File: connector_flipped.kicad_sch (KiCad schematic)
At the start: 4 parts, among them J1 Screw_Terminal_01x04

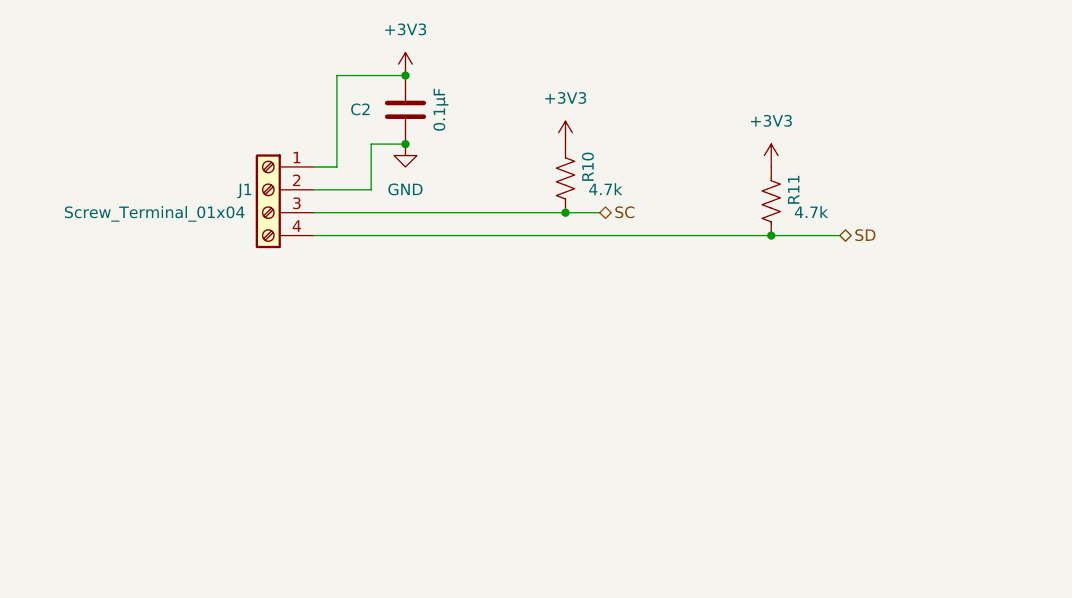
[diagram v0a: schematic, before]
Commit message: four sensor connectors flipped to the way they should be installed.
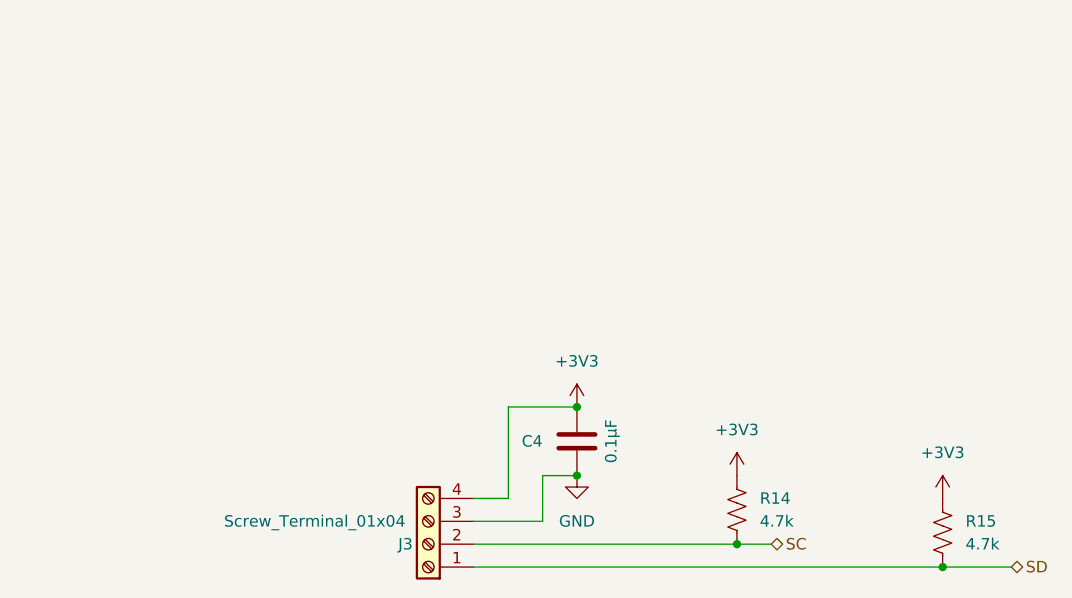
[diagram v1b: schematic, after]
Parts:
- removed C2: 0.1µF, ProjectLib:C_0402_1005Metric, symbol ProjectLib:C
- removed J1: Screw_Terminal_01x04, ProjectLib:TerminalBlock_Phoenix_MPT-0,5-4-2.54_1x04_P2.54mm_Horizontal, symbol ProjectLib:Screw_Terminal_01x04
- removed R10, R11: 4.7k, ProjectLib:R_0402_1005Metric, symbol ProjectLib:R_US
- added C4: 0.1µF, ProjectLib:C_0402_1005Metric, symbol ProjectLib:C
- added J3: Screw_Terminal_01x04, ProjectLib:TerminalBlock_Phoenix_MPT-0,5-4-2.54_1x04_P2.54mm_Horizontal, symbol ProjectLib:Screw_Terminal_01x04
- added R14, R15: 4.7k, ProjectLib:R_0402_1005Metric, symbol ProjectLib:R_US
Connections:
- net +3V3: now also C4.1, J3.4 (Pin_4), R14.1, R15.1
- net GND: now also C4.2, J3.3 (Pin_3)
- net SC: now also J3.2 (Pin_2), R14.2
- net SD: now also J3.1 (Pin_1), R15.2

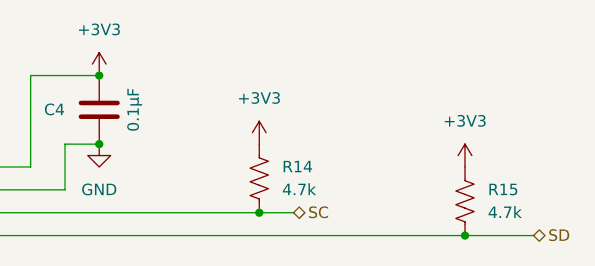
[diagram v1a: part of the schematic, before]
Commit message: changed single 10k pull-up to 4.7k like others. Renumbered components to fill numbering gaps.
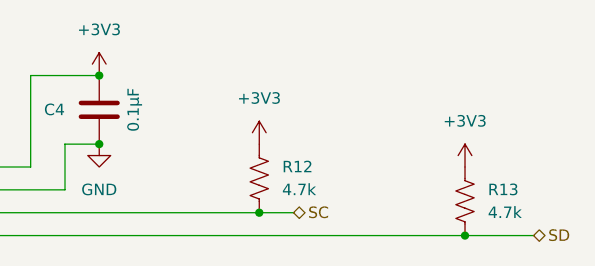
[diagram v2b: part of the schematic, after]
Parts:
- renumbered R14 to R12, R15 to R13
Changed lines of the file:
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@@
 		(dnp no)
 		(fields_autoplaced yes)
-		(property "Reference" "R14"
+		(property "Reference" "R12"
 			(at 124.46 78.7399 0)
 			(effects
@@
 			(project "multiplexI2C"
 				(path "/0c2d0c14-8850-4a30-bb78-b2f40cb442ba/0ffcdb2c-d74e-4b7d-b16c-7be1edbff217"
-					(reference "R24")
+					(reference "R22")
 					(unit 1)
 				)
 				(path "/0c2d0c14-8850-4a30-bb78-b2f40cb442ba/a879a04a-2836-4e79-a27d-1b46398578a8"
-					(reference "R22")
+					(reference "R20")
 					(unit 1)
 				)
 				(path "/0c2d0c14-8850-4a30-bb78-b2f40cb442ba/c4c0e226-9808-439f-a0d2-8470ea18ef3d"
+					(reference "R12")
+					(unit 1)
+				)
+				(path "/0c2d0c14-8850-4a30-bb78-b2f40cb442ba/fd54f7e6-e57e-45a8-af7b-068cfabb882f"
 					(reference "R14")
-					(unit 1)
-				)
-				(path "/0c2d0c14-8850-4a30-bb78-b2f40cb442ba/fd54f7e6-e57e-45a8-af7b-068cfabb882f"
-					(reference "R16")
 					(unit 1)
 				)
@@
 		(dnp no)
 		(fields_autoplaced yes)
-		(property "Reference" "R15"
+		(property "Reference" "R13"
 			(at 147.32 81.2799 0)
 			(effects
@@
 			(project "multiplexI2C"
 				(path "/0c2d0c14-8850-4a30-bb78-b2f40cb442ba/0ffcdb2c-d74e-4b7d-b16c-7be1edbff217"
-					(reference "R25")
+					(reference "R23")
 					(unit 1)
 				)
 				(path "/0c2d0c14-8850-4a30-bb78-b2f40cb442ba/a879a04a-2836-4e79-a27d-1b46398578a8"
-					(reference "R23")
+					(reference "R21")
 					(unit 1)
 				)
 				(path "/0c2d0c14-8850-4a30-bb78-b2f40cb442ba/c4c0e226-9808-439f-a0d2-8470ea18ef3d"
+					(reference "R13")
+					(unit 1)
+				)
+				(path "/0c2d0c14-8850-4a30-bb78-b2f40cb442ba/fd54f7e6-e57e-45a8-af7b-068cfabb882f"
 					(reference "R15")
 					(unit 1)
 				)
-				(path "/0c2d0c14-8850-4a30-bb78-b2f40cb442ba/fd54f7e6-e57e-45a8-af7b-068cfabb882f"
-					(reference "R17")
-					(unit 1)
-				)

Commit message: cleaned up fab layer annotation.
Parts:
- C4, R12, R13: Notes (none) -> or equivalent
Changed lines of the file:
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@@
 			)
 		)
-		(property "Notes" ""
+		(property "Notes" "or equivalent"
+			(at 104.14 72.39 0)
+			(effects
+				(font
+					(size 1.27 1.27)
+				)
+				(hide yes)
+			)
+		)
+		(property "Manuf Part" ""
+			(at 104.14 72.39 0)
+			(effects
+				(font
+					(size 1.27 1.27)
+				)
+				(hide yes)
+			)
+		)
+		(property "Manuf Series" ""
 			(at 104.14 72.39 0)
 			(effects
@@
 		)
 		(property "Notes" "or equivalent"
+			(at 87.63 83.82 0)
+			(effects
+				(font
+					(size 1.27 1.27)
+				)
+				(hide yes)
+			)
+		)
+		(property "Manuf Part" ""
+			(at 87.63 83.82 0)
+			(effects
+				(font
+					(size 1.27 1.27)
+				)
+				(hide yes)
+			)
+		)
+		(property "Manuf Series" ""
 			(at 87.63 83.82 0)
 			(effects
@@
 			)
 		)
-		(property "Notes" ""
+		(property "Notes" "or equivalent"
+			(at 121.92 80.01 0)
+			(effects
+				(font
+					(size 1.27 1.27)
+				)
+				(hide yes)
+			)
+		)
+		(property "Manuf Part" ""
+			(at 121.92 80.01 0)
+			(effects
+				(font
+					(size 1.27 1.27)
+				)
+				(hide yes)
+			)
+		)
+		(property "Manuf Series" ""
 			(at 121.92 80.01 0)
 			(effects
@@
 			)
 		)
-		(property "Notes" ""
-			(at 144.78 82.55 0)
-			(effects
+		(property "Notes" "or equivalent"
+			(at 144.78 82.55 0)
+			(effects
+				(font
+					(size 1.27 1.27)
+				)
+				(hide yes)
+			)
+		)
+		(property "Manuf Part" ""
+			(at 144.78 82.55 0)
+			(effects
+				(font
+					(size 1.27 1.27)
+				)
+				(hide yes)
+			)
+		)
+		(property "Manuf Series" ""
+			(at 144.78 82.55 0)
+			(effects

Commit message: ongoing.
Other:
- title: Multiplex I2C to Screw Terminal connectors -> Screw Terminal connector flipped
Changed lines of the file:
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@@
 	(paper "A4")
 	(title_block
-		(title "Multiplex I2C to Screw Terminal connectors")
-		(date "2025-09-07")
-		(rev "v0.2.0")
+		(title "Screw Terminal connector flipped")
+		(date "2025-11-29")
+		(rev "v0.2.2")
 	)
 	(junction

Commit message: ongoing cleanup for submit.
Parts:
- C4: Package (none) -> C_0402_1005Metric
- J3: Package (none) -> 1x04_P2.54mm_Horizontal
- R12, R13: Package (none) -> R_0402_1005Metric
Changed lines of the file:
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@@
 			)
 		)
-		(property "Datasheet" "~"
+		(property "Datasheet" ""
 			(at 104.14 72.39 0)
 			(effects
@@
 		)
 		(property "Manuf Series" ""
+			(at 104.14 72.39 0)
+			(effects
+				(font
+					(size 1.27 1.27)
+				)
+				(hide yes)
+			)
+		)
+		(property "Package" "C_0402_1005Metric"
 			(at 104.14 72.39 0)
 			(effects
@@
 			)
 		)
-		(property "Datasheet" "~"
-			(at 87.63 83.82 0)
-			(effects
-				(font
-					(size 1.27 1.27)
-				)
-				(hide yes)
-			)
-		)
-		(property "Description" "Generic screw terminal, single row, 01x04, script generated (kicad-library-utils/schlib/autogen/connector/)"
+		(property "Datasheet" "https://www.lcsc.com/datasheet/C474920.pdf"
+			(at 87.63 83.82 0)
+			(effects
+				(font
+					(size 1.27 1.27)
+				)
+				(hide yes)
+			)
+		)
+		(property "Description" "Generic screw terminal, single row, 01x04"
 			(at 87.63 83.82 0)
 			(effects
@@
 		)
 		(property "Manuf Series" ""
+			(at 87.63 83.82 0)
+			(effects
+				(font
+					(size 1.27 1.27)
+				)
+				(hide yes)
+			)
+		)
+		(property "Package" "1x04_P2.54mm_Horizontal"
 			(at 87.63 83.82 0)
 			(effects
@@
 			)
 		)
-		(property "Datasheet" "~"
+		(property "Datasheet" ""
 			(at 121.92 80.01 0)
 			(effects
@@
 		)
 		(property "Manuf Series" ""
+			(at 121.92 80.01 0)
+			(effects
+				(font
+					(size 1.27 1.27)
+				)
+				(hide yes)
+			)
+		)
+		(property "Package" "R_0402_1005Metric"
 			(at 121.92 80.01 0)
 			(effects
@@
 			)
 		)
-		(property "Datasheet" "~"
+		(property "Datasheet" ""
 			(at 144.78 82.55 0)
 			(effects
@@
 			(at 144.78 82.55 0)
 			(effects
+				(font
+					(size 1.27 1.27)
+				)
+				(hide yes)
+			)
+		)
+		(property "Package" "R_0402_1005Metric"
+			(at 144.78 82.55 0)
+			(effects
